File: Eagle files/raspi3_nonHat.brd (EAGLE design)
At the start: 58.4 x 61.9 mm, 23 parts, among them IC5 PAM8403, K1 PIN20X2

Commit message: 30-eagle
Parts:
- moved R3 81.8 mm to (50.8, 11.4), turned to 270 degrees
- moved OLED_MODULE 80.1 mm to (69.8, 31.8)
- moved SPEAKER 75.5 mm to (77.5, 53.3)
- moved LED1 72.7 mm to (50.8, 3.81)
- moved R1 59.9 mm to (50.8, 31.8), turned to 270 degrees
- moved R2 57.1 mm to (50.8, 21.6), turned to 270 degrees
- moved EN2 51.4 mm to (69.2, 7.62)
- moved C6 50.8 mm to (73.0, 12.1)
- moved C4 50.8 mm to (64.8, 5.71)
- moved R8 50.8 mm to (70.5, 10.2)
- moved C5 50.8 mm to (64.8, 8.89)
- moved R6 50.8 mm to (62.9, 3.81)
- moved R7 50.8 mm to (62.9, 11.4)
- moved SL2 50.8 mm to (81.3, 7.62)
- moved C16 26.2 mm to (34.3, 55.9)
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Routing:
- net CLK: track 22.3 -> 21.1 mm
- net GND: track 32.9 -> 31.6 mm
- net DT: track 23.4 -> 22.2 mm
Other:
- board size 58.4 x 61.9 mm -> 63.5 x 60.6 mm

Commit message: 30-eagle2
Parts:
- removed SL2: (no value), con-amp-quick:05P
- turned C30 to 180 degrees
- turned LED1 to 180 degrees
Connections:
- removed net C16: C16.2
- net +5V: no longer SL2.5
- net CLK: no longer SL2.1
- net DT: no longer SL2.2
- net GND: now also C16.2; no longer SL2.4
- net SW: no longer SL2.3
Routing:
- net GND: track 31.6 -> 182.0 mm
- net +5V: track 33.7 -> 115.3 mm
- net +3V3: track 0.00 -> 69.5 mm
- net N$4: track 0.00 -> 66.9 mm
- net N$29: track 0.00 -> 51.1 mm
- net SDA: track 0.00 -> 41.2 mm
- net SCL: track 0.00 -> 32.8 mm
- net CLK: track 21.1 -> 12.8 mm
- net N$1: track 0.00 -> 4.34 mm
- net N$34: track 0.00 -> 3.49 mm
- net SW: track 13.5 -> 10.3 mm
- net DT: track 22.2 -> 19.6 mm

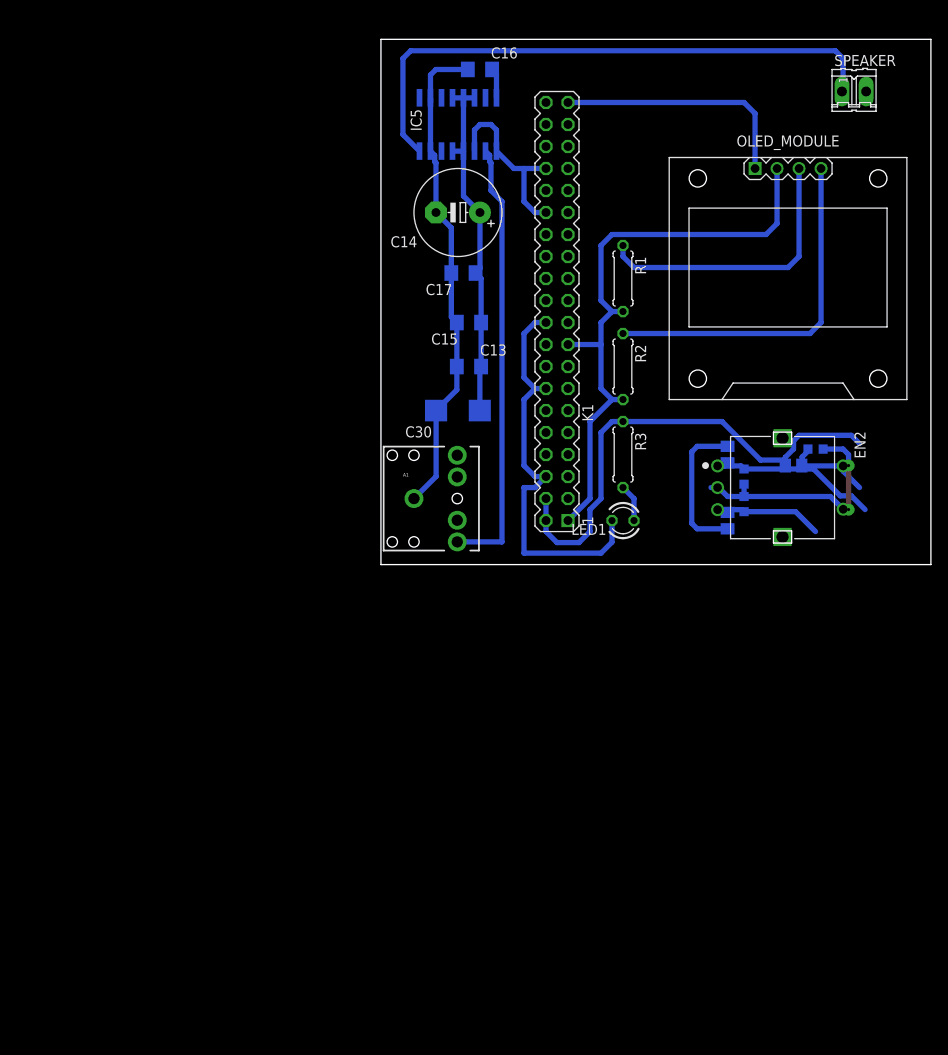
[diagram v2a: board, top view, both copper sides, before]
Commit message: added ads1115
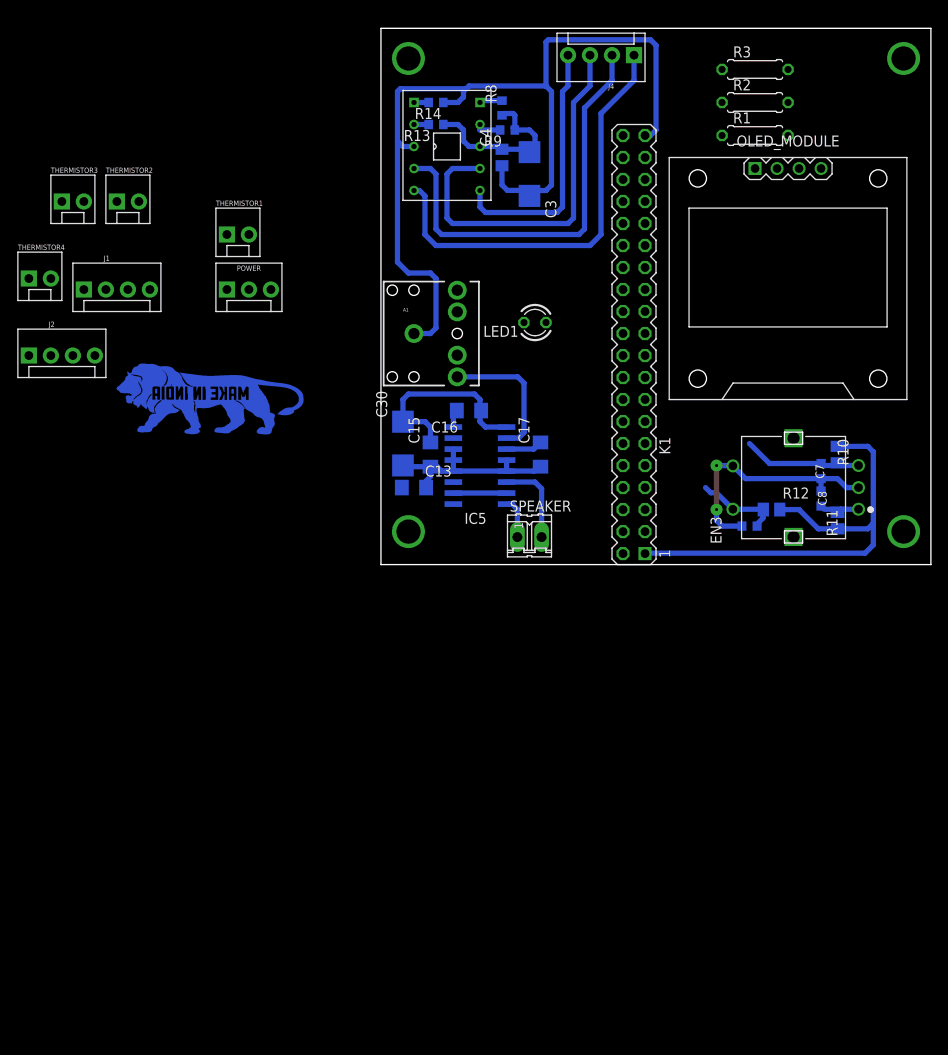
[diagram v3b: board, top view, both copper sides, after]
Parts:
- removed C14: 470uF, resistor:E5-10,5
- removed C5, C6: (no value), adafruit:C0603K
- removed EN2: PEC11L-4220F-S0015, Encoders:PEC11L-4220F-S0015
- removed R6, R7: (no value), rcl:M0805
- added C3: 10u, CEDT_JANUARY_2015_v5:C/6032-28R
- added C7, C8, C9: (no value), adafruit:C0603K
- added EN3: PEC11L-4220F-S0015, Encoders:PEC11L-4220F-S0015
- added J1, J2, J4: (no value), SparkFun-Connectors:MOLEX-1X4
- added POWER: (no value), SparkFun-Connectors:MOLEX-1X3
- added R10, R11, R12: (no value), rcl:M0805
- added R13, R14, R9: 10k, CEDT_JANUARY_2015_v5:R0603
- added THERMISTOR1, THERMISTOR2, THERMISTOR3, THERMISTOR4: (no value), SparkFun-Connectors:MOLEX-1X2
- added U$1: MAKE-IN-INDIA-LOGO, namanpuri:MAKE-IN-INDIA
- added U$3: BOB_10PIN, CEDT_JANUARY_2015_v5:BOB10
- C4: value (none) -> 0.1u; device adafruit:C0603K -> CEDT_JANUARY_2015_v5:C0805
- R8: value (none) -> 10k; device rcl:M0805 -> CEDT_JANUARY_2015_v5:R0603
- moved SPEAKER 63.6 mm to (40.0, 1.91)
- moved R8 53.3 mm to (36.8, 51.4), turned to 270 degrees
- moved C4 48.8 mm to (36.8, 45.7), turned to 270 degrees
- moved R3 47.0 mm to (66.0, 55.9), turned to 0 degrees
- moved IC5 39.5 mm to (34.3, 10.2), turned to 90 degrees
- moved C16 39.4 mm to (33.0, 16.5), turned to 180 degrees
- moved R2 34.1 mm to (66.0, 52.1), turned to 0 degrees
- moved LED1 25.0 mm to (40.6, 26.7)
- moved C17 22.8 mm to (41.3, 11.4), turned to 270 degrees
- moved R1 22.5 mm to (66.0, 48.3), turned to 0 degrees
- moved A1 19.0 mm to (26.7, 25.4)
- moved C15 15.9 mm to (28.6, 11.4), turned to 270 degrees
- moved C13 15.3 mm to (26.7, 7.62)
- moved K1 9.67 mm to (52.1, 24.1)
- moved C30 7.41 mm to (25.4, 12.7), turned to 270 degrees
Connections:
- new net 0CS0: J2.1, K1.24
- new net 0CS1: K1.26
- new net 0MISO: J2.4, K1.21
- new net 0MOSI: J2.3, K1.19
- new net 0SCLK: J2.2, K1.23
- new net 1CS0: J1.1, K1.36
- new net 1MISO: J1.4, K1.35
- new net 1MOSI: J1.3, K1.38
- new net 1SCLK: J1.2, K1.40
- new net AIN0: J4.2, U$3.4
- new net AIN1: J4.1, U$3.5
- new net AIN2: J4.4, U$3.6
- new net AIN3: J4.3, U$3.7
- new net N$12: R8.1, U$3.10
- new net N$13: R9.1, U$3.9
- new net N$14: R13.1, U$3.2
- new net N$15: R14.1, U$3.1
- new net RX: K1.10, THERMISTOR4.2
- new net TX: K1.8, THERMISTOR4.1
- net +3V3: now also C3.+, C4.1, POWER.2, R10.2, R11.2, R12.1, R13.2, R8.2, R9.2, THERMISTOR2.1, U$3.8
- net +5V: now also POWER.3, THERMISTOR3.1; no longer C14.+, R6.2, R7.2, R8.1
- net CLK: now also C7.1, EN3.B, R10.1; no longer C4.1, EN2.B, R6.1
- net DT: now also C8.1, EN3.A, R11.1; no longer C5.1, EN2.A, R7.1
- net GND: now also C3.-, C7.2, C8.2, C9.2, EN3.2, EN3.C, POWER.1, R14.2, THERMISTOR2.2, THERMISTOR3.2, U$3.3; no longer C14.-, C5.2, C6.2, EN2.2, EN2.C
- net SCL: now also K1.5, THERMISTOR1.1
- net SDA: now also K1.3, THERMISTOR1.2
- net SW: now also C9.1, EN3.1, R12.2; no longer C6.1, EN2.1, R8.2
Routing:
- net +5V: track 115.3 -> 22.9 mm
- net N$4: track 66.9 -> 4.70 mm
- net AIN1: track 0.00 -> 49.6 mm
- net AIN0: track 0.00 -> 48.2 mm
- net AIN3: track 0.00 -> 43.9 mm
- net SDA: track 41.2 -> 0.00 mm
- net N$29: track 51.1 -> 16.0 mm
- net SCL: track 32.8 -> 0.00 mm
- net AIN2: track 0.00 -> 29.7 mm
- net DT: track 19.6 -> 4.48 mm
- net GND: track 182.0 -> 169.2 mm
- net N$27: track 0.00 -> 9.94 mm
- net +3V3: track 69.5 -> 74.3 mm
- net N$1: track 4.34 -> 0.00 mm
- net N$13: track 0.00 -> 2.96 mm
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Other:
- board size 63.5 x 60.6 mm -> 63.5 x 61.9 mm
